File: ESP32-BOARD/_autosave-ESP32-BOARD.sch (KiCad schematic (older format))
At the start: 152 parts, among them J101 Screw_Terminal_01x08, J102 Screw_Terminal_01x08, J103 Screw_Terminal_01x08, J104 Screw_Terminal_01x08, J105 Input_01x02, J106 Screw_Terminal_01x04, J120 Conn_01x07_Male, Q101 BT136-600, Q102 BT136-600, Q103 BT136-600, Q104 BT136-600, U101 LM358, U102 LM358, U103 LM2596S-ADJ, U104 LM2596S-ADJ, U105 TLP290-4, U106 TLP290-4, U107 KAQY214S, U108 KAQY214S, U109 MOC3023S, U110 MOC3023S, U111 MOC3023S, U112 MOC3023S, U113 SIM800L, U114 ESP32-dev-board

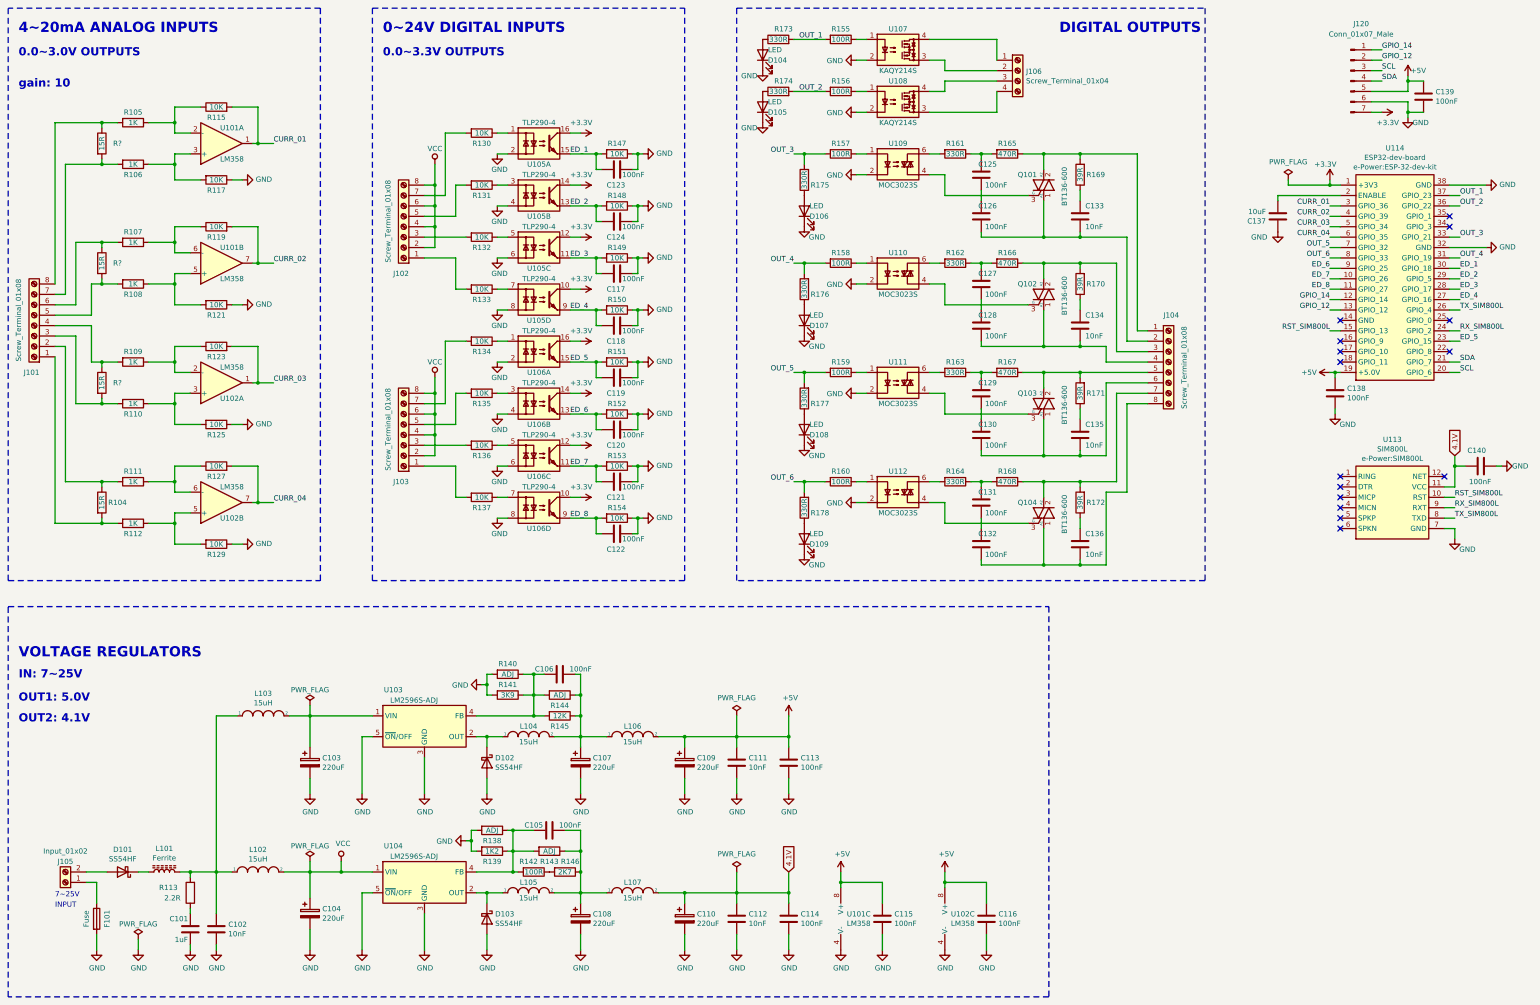
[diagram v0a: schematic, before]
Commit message: arrumei as dimensoes dos furos
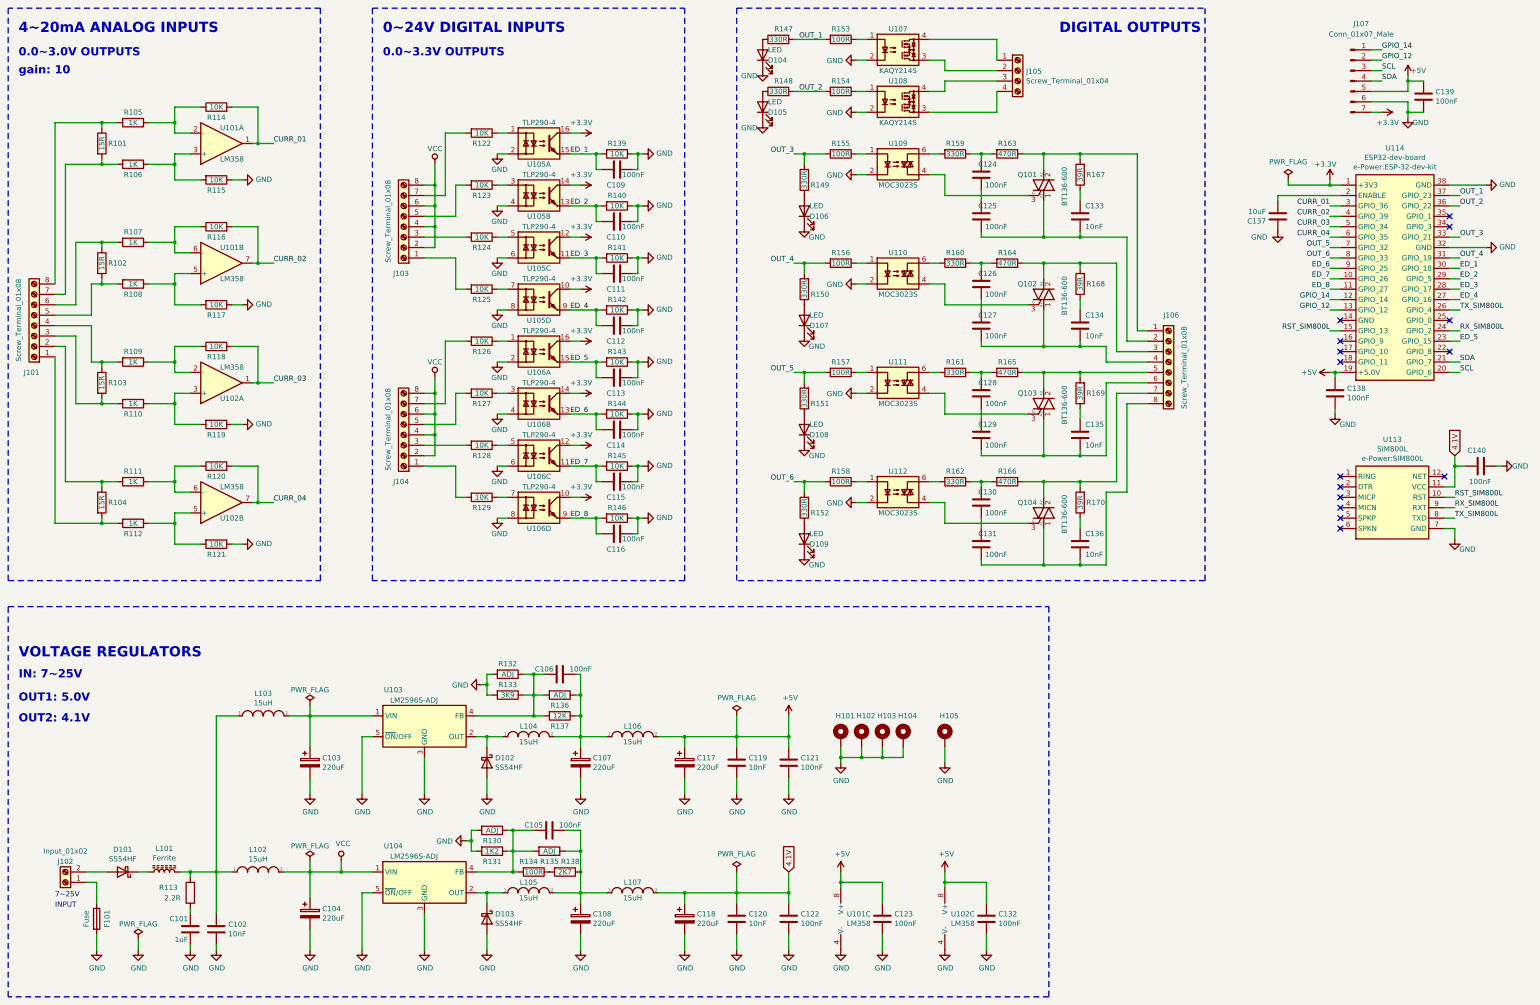
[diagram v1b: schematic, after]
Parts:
- added H101, H102, H103, H104: MountingHole_Pad, e-Power:MountingHole_4mm_Pad_Via, symbol Mechanical:MountingHole_Pad
- added H105: MountingHole_Pad, e-Power:MountingHole_3.2mm_M3_Pad, symbol Mechanical:MountingHole_Pad
- gave numbers to parts that had none: 3
- renumbered C123 to C109, C124 to C110, C117 to C111, C118 to C112, C119 to C113, C120 to C114, C121 to C115, C122 to C116, C109 to C117, C110 to C118, C111 to C119, C112 to C120, C113 to C121, C114 to C122, C115 to C123, C125 to C124, C126 to C125, C127 to C126, C128 to C127, C129 to C128, C130 to C129, C131 to C130, C132 to C131, C116 to C132, J105 to J102, J102 to J103, J103 to J104, J106 to J105, J104 to J106, J120 to J107, R115 to R114, R117 to R115, R119 to R116, R121 to R117, R123 to R118, R125 to R119, R127 to R120, R129 to R121, R130 to R122, R131 to R123, R132 to R124, R133 to R125, R134 to R126, R135 to R127, R136 to R128, R137 to R129, R138 to R130, R139 to R131, R140 to R132, R141 to R133, R142 to R134, R143 to R135, R144 to R136, R145 to R137, R146 to R138, R147 to R139, R148 to R140, R149 to R141, R150 to R142, R151 to R143, R152 to R144, R153 to R145, R154 to R146, R173 to R147, R174 to R148, R175 to R149, R176 to R150, R177 to R151, R178 to R152, R155 to R153, R156 to R154, R157 to R155, R158 to R156, R159 to R157, R160 to R158, R161 to R159, R162 to R160, R163 to R161, R164 to R162, R165 to R163, R166 to R164, R167 to R165, R168 to R166, R169 to R167, R170 to R168, R171 to R169, R172 to R170
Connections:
- net GND: now also H101.1, H102.1, H103.1, H104.1, H105.1
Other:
- note added: "gain: 10\n\n\n"
- note removed: "gain: 10\n\n"

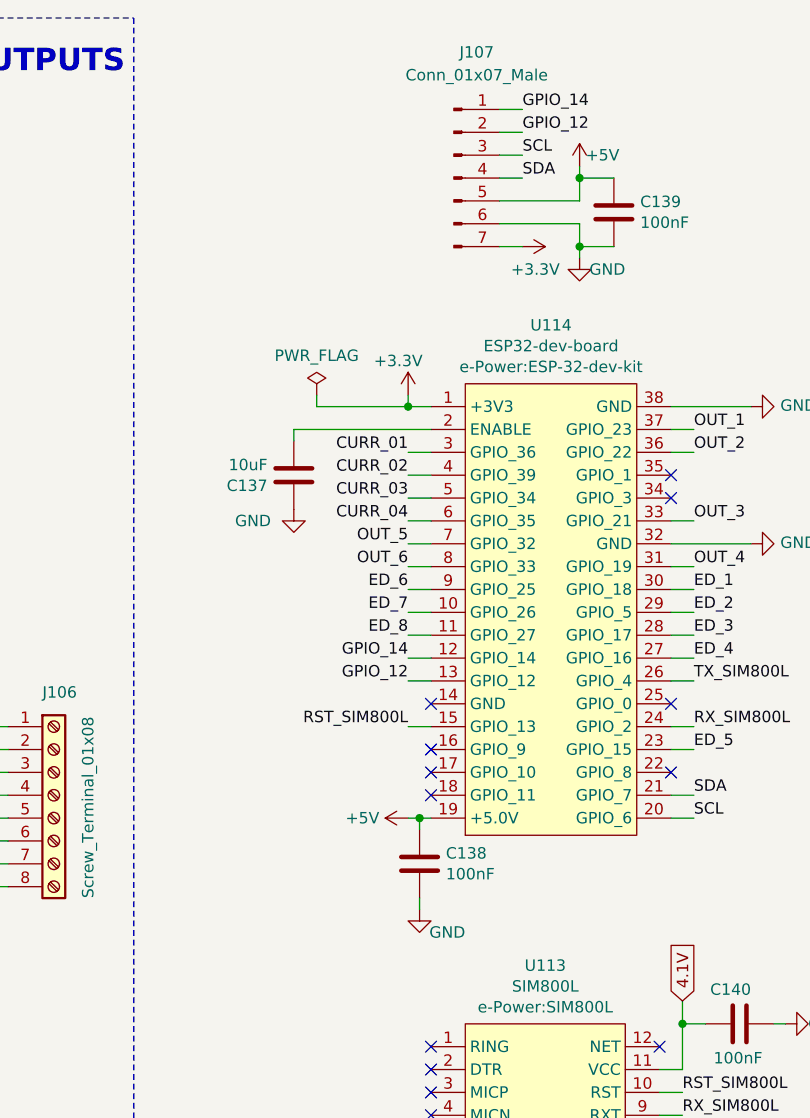
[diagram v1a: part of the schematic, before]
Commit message: changes de boards to 4 layers
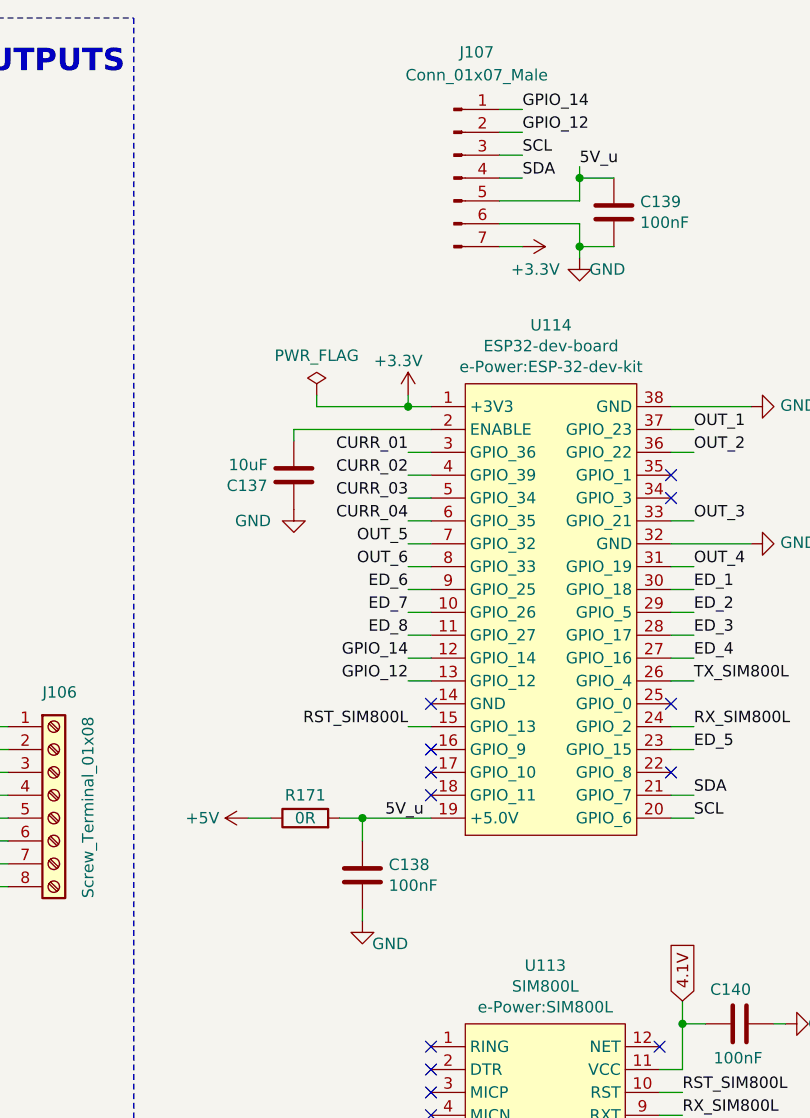
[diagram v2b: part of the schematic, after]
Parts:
- added R171: 0R, Resistor_SMD:R_0805_2012Metric, symbol Device:R
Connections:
- net +5V: now also R171.1; no longer C138.1, C139.1, J107.5 (Pin_5), U114.19 (+5.0V)
- new net 5V_u: C138.1, C139.1, J107.5 (Pin_5), R171.2, U114.19 (+5.0V)
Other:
- moved on the sheet: C138
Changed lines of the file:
@@
 L power:+5V #PWR0175
 U 1 1 5EF030E8
-P 13700 4500
-F 0 "#PWR0175" H 13700 4350 50  0001 C CNN
-F 1 "+5V" V 13700 4700 50  0000 C CNN
-F 2 "" H 13700 4500 50  0001 C CNN
-F 3 "" H 13700 4500 50  0001 C CNN
-	1    13700 4500
+P 13000 4500
+F 0 "#PWR0175" H 13000 4350 50  0001 C CNN
+F 1 "+5V" V 13000 4700 50  0000 C CNN
+F 2 "" H 13000 4500 50  0001 C CNN
+F 3 "" H 13000 4500 50  0001 C CNN
+	1    13000 4500
 	0    -1   -1   0
 $EndComp
-Wire Wire Line
-	13700 4500 13750 4500
 $Comp
 L power:+3.3V #PWR0174
@@
 $EndComp
 $Comp
-L power:+5V #PWR0178
-U 1 1 5F9DD3E9
-P 14450 1650
-F 0 "#PWR0178" H 14450 1500 50  0001 C CNN
-F 1 "+5V" H 14550 1700 50  0000 C CNN
-F 2 "" H 14450 1650 50  0001 C CNN
-F 3 "" H 14450 1650 50  0001 C CNN
-	1    14450 1650
-	1    0    0    -1
-$EndComp
-$Comp
 L power:GND #PWR0179
 U 1 1 5F9DE9D7
@@
 L Device:C C138
 U 1 1 5FA6F37C
-P 13750 4700
-F 0 "C138" H 13865 4746 50  0000 L CNN
-F 1 "100nF" H 13865 4655 50  0000 L CNN
-F 2 "Capacitor_SMD:C_0805_2012Metric" H 13788 4550 50  0001 C CNN
-F 3 "https://datasheet.lcsc.com/szlcsc/Samsung-Electro-Mechanics-CL21B103KBANNNC_C1710.pdf" H 13750 4700 50  0001 C CNN
-F 4 "C49678" H 13750 4700 50  0001 C CNN "LCSC"
-	1    13750 4700
-	1    0    0    -1
-$EndComp
-Wire Wire Line
-	13750 4550 13750 4500
-Connection ~ 13750 4500
-Wire Wire Line
-	13750 4500 13800 4500
+P 13500 4750
+F 0 "C138" H 13615 4796 50  0000 L CNN
+F 1 "100nF" H 13615 4705 50  0000 L CNN
+F 2 "Capacitor_SMD:C_0805_2012Metric" H 13538 4600 50  0001 C CNN
+F 3 "https://datasheet.lcsc.com/szlcsc/Samsung-Electro-Mechanics-CL21B103KBANNNC_C1710.pdf" H 13500 4750 50  0001 C CNN
+F 4 "C49678" H 13500 4750 50  0001 C CNN "LCSC"
+	1    13500 4750
+	1    0    0    -1
+$EndComp
+Connection ~ 13500 4500
 $Comp
 L Device:C C139
@@
 L power:GND #PWR0176
 U 1 1 5FBD44B2
-P 13750 4900
-F 0 "#PWR0176" H 13750 4650 50  0001 C CNN
-F 1 "GND" H 13950 4800 50  0000 R CNN
-F 2 "" H 13750 4900 50  0001 C CNN
-F 3 "" H 13750 4900 50  0001 C CNN
-	1    13750 4900
-	1    0    0    -1
-$EndComp
-Wire Wire Line
-	13750 4900 13750 4850
+P 13500 4950
+F 0 "#PWR0176" H 13500 4700 50  0001 C CNN
+F 1 "GND" H 13700 4850 50  0000 R CNN
+F 2 "" H 13500 4950 50  0001 C CNN
+F 3 "" H 13500 4950 50  0001 C CNN
+	1    13500 4950
+	1    0    0    -1
+$EndComp
+Wire Wire Line
+	13500 4950 13500 4900
 $Comp
 L power:GND #PWR0180
@@
 Wire Wire Line
 	10000 8250 10000 8100
+$Comp
+L Device:R R171
+U 1 1 5F574CA2
+P 13250 4500
+F 0 "R171" V 13350 4500 50  0000 C CNN
+F 1 "0R" V 13250 4500 50  0000 C CNN
+F 2 "Resistor_SMD:R_0805_2012Metric" V 13180 4500 50  0001 C CNN
+F 3 "" H 13250 4500 50  0001 C CNN
+F 4 "C17477" H 13250 4500 50  0001 C CNN "LCSC"
+	1    13250 4500
+	0    -1   -1   0
+$EndComp
+Wire Wire Line
+	13000 4500 13100 4500
+Wire Wire Line
+	13400 4500 13500 4500
+Wire Wire Line
+	13500 4500 13500 4600
+Text Label 13600 4500 0    50   ~ 0
+5V_u
+Wire Wire Line
+	13500 4500 13800 4500
+Text Label 14450 1650 0    50   ~ 0
+5V_u
 $EndSCHEMATC
